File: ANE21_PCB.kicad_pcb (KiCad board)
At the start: 4 copper layers, 59.3 x 63.9 mm, 61 parts, among them J1 Conn_01x02, J13 1-2199119-5, J2 2036150003 (USB-C_Connector), J3 USB-A-S-VT, J5 690-019-298-412, J6 Conn_02x07_Odd_Even, J7 2036150003 (USB-C_Connector), U1 74LVC1G07SE-7, U10 PUSB3FR4, U11 TPD4EUSB30, U12 SI-51005-F, U13 RT9742SNGV, U2 74LVC1G07SE-7, U3 HUSB238_xxxDD, U4 AP62300WU-7, U8 AP62300WU-7, U9 PUSB3FR4

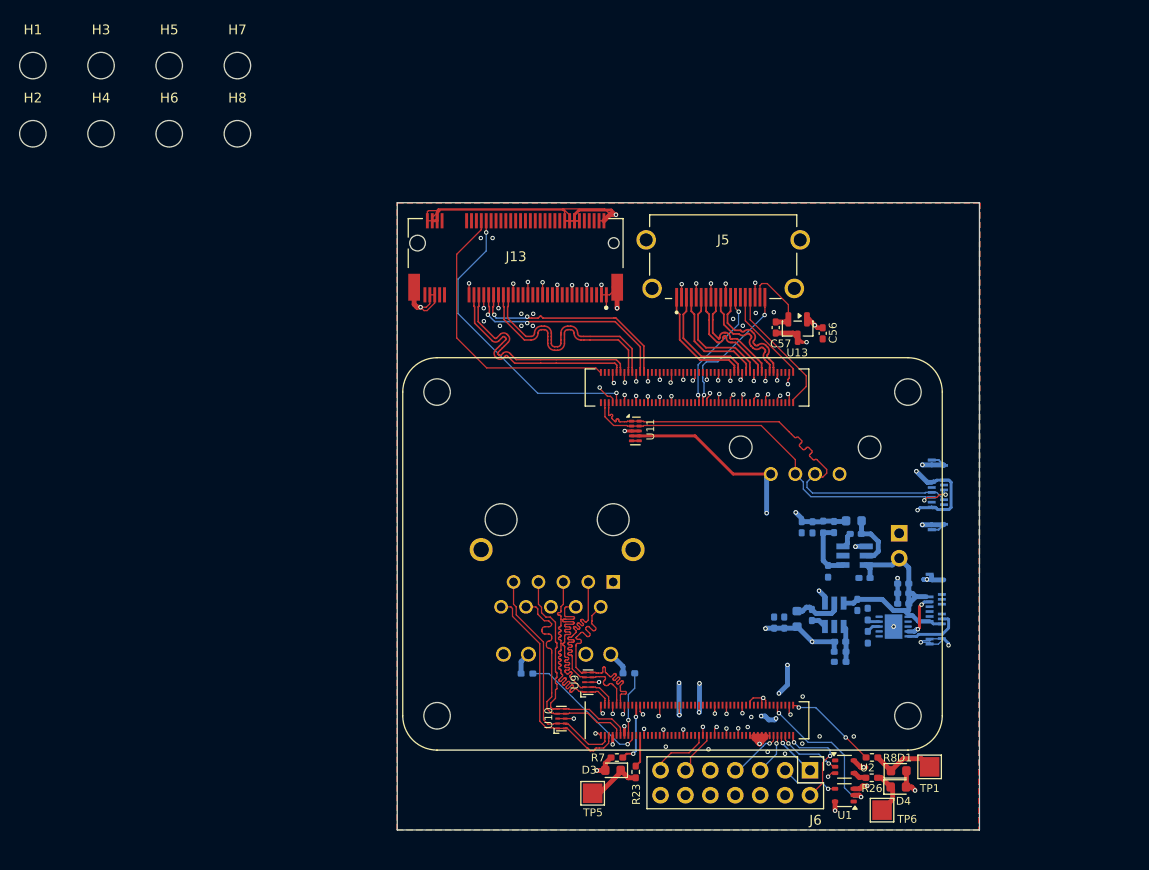
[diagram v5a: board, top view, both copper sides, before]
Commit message: Changed quite a bit, PCB smoll now
Redid all traces, replaced HUSB238 with ch224k, made PCB even smaller.
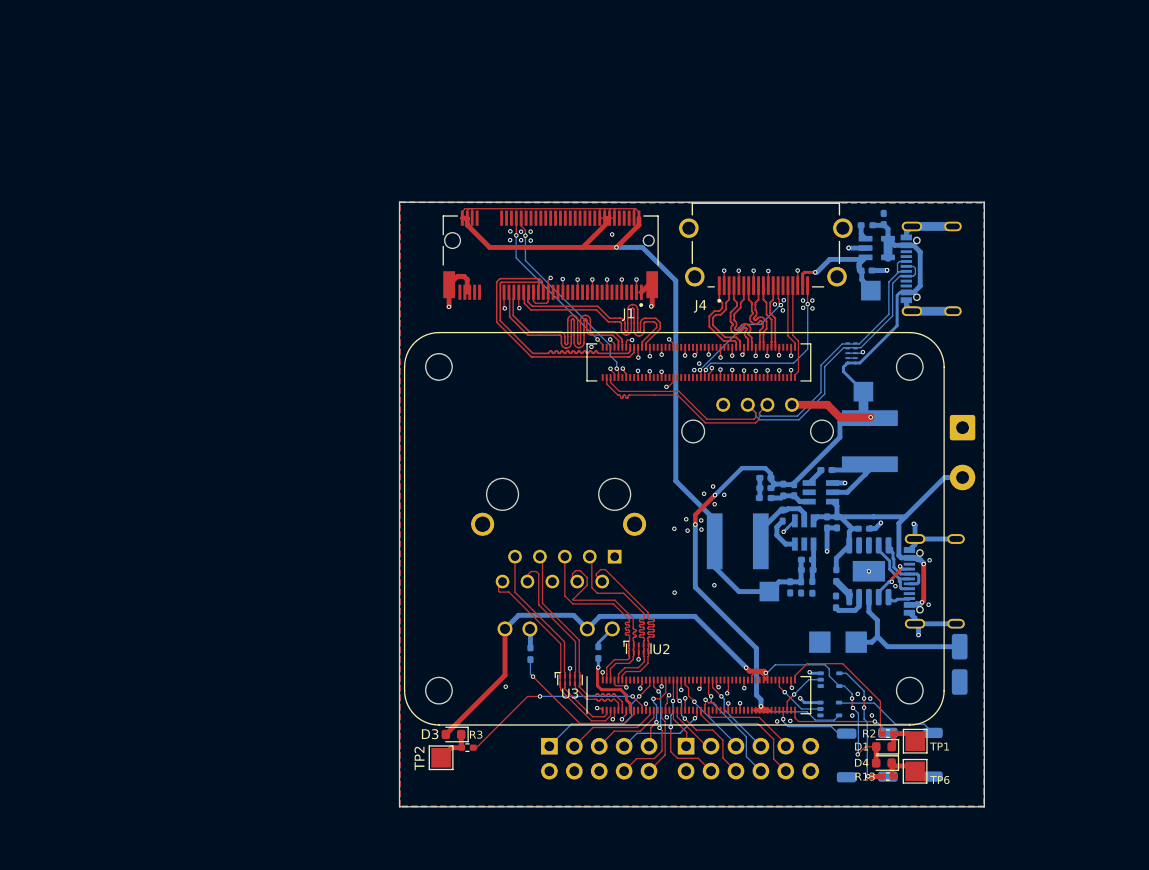
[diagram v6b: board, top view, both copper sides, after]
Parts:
- removed C3: 1µF, Capacitor_SMD:C_0402_1005Metric_Pad0.74x0.62mm_HandSolder
- removed C4, C5: 10µF, Capacitor_SMD:C_0402_1005Metric_Pad0.74x0.62mm_HandSolder
- removed C56, C57: 100n, Capacitor_SMD:C_0402_1005Metric_Pad0.74x0.62mm_HandSolder
- removed H1, H2, H3, H4, H5, H6, H7, H8: MountingHole, MountingHole:MountingHole_2.7mm_M2.5
- removed J13: 1-2199119-5, M2Key:TE_1-2199119-5
- removed J7: 2036150003 (USB-C_Connector), USB-C:CONN_2036150003_MOL(USB-c_connector)
- removed R15, R16: 330, Resistor_SMD:R_0402_1005Metric_Pad0.72x0.64mm_HandSolder
- removed R23, R26, R8: 1k, Resistor_SMD:R_0402_1005Metric_Pad0.72x0.64mm_HandSolder
- removed R7: 10k, Resistor_SMD:R_0402_1005Metric_Pad0.72x0.64mm_HandSolder
- removed U13: RT9742SNGV, Package_TO_SOT_SMD:SOT-23
- added C14: C, Capacitor_SMD:C_0402_1005Metric_Pad0.74x0.62mm_HandSolder, B.Cu at (100.7, 88.2)
- added C15: C, Capacitor_SMD:C_0402_1005Metric_Pad0.74x0.62mm_HandSolder, B.Cu at (101.8, 88.2)
- added C16: 100nF, Capacitor_SMD:C_0402_1005Metric_Pad0.74x0.62mm_HandSolder, B.Cu at (108.2, 82.2)
- added C17: C_Polarized 100uF, Capacitor_SMD:CP_Elec_4x3, B.Cu at (118.0, 96.1)
- added CR1: SMBJ15A, footprints:DIODE_DO214AA, B.Cu at (105.6, 93.8)
- added J4: HDMI_A_1.4, HMDI:AMPHENOL_10029449-111RLF, F.Cu at (98.2, 51.6)
- added J8: Conn_02x06_Odd_Even, Connector_PinHeader_2.54mm:PinHeader_2x06_P2.54mm_Vertical, B.Cu at (90.1, 104.4)
- added R10: R, Resistor_SMD:R_0402_1005Metric_Pad0.72x0.64mm_HandSolder, B.Cu at (98.2, 79.1)
- added R11: R, Resistor_SMD:R_0402_1005Metric_Pad0.72x0.64mm_HandSolder, B.Cu at (102.5, 86.4)
- added R12: R, Resistor_SMD:R_0402_1005Metric_Pad0.72x0.64mm_HandSolder, B.Cu at (103.0, 88.2)
- added R13: R, Resistor_SMD:R_0402_1005Metric_Pad0.72x0.64mm_HandSolder, F.Cu at (110.7, 107.5)
- added R14: 10k, Resistor_SMD:R_0402_1005Metric_Pad0.72x0.64mm_HandSolder, B.Cu at (105.4, 87.0)
- added R9: R, Resistor_SMD:R_0402_1005Metric_Pad0.72x0.64mm_HandSolder, B.Cu at (100.0, 78.3)
- added SW1: SW_Push, Button_Switch_SMD:SW_SPST_TS-1088-xR020, B.Cu at (115.3, 105.3)
- added SW2: SW_Push, Button_Switch_SMD:SW_SPST_TS-1088-xR020, B.Cu at (110.7, 105.3)
- added SW3: SW_Push, Button_Switch_SMD:SW_SPST_TS-1088-xR020, B.Cu at (106.5, 105.3)
- added TP2: TestPoint, TestPoint:TestPoint_Pad_2.0x2.0mm, F.Cu at (65.1, 105.6)
- added TP3: TestPoint, TestPoint:TestPoint_Pad_2.0x2.0mm, B.Cu at (109.0, 58.0)
- added TP4: TestPoint, TestPoint:TestPoint_Pad_2.0x2.0mm, B.Cu at (108.2, 68.3)
- added U5: NCP380HSN05AAT1G, NCP380HSN05AAT1G:SOT95P275X120-5N, B.Cu at (109.6, 53.6)
- added U7: AP62300WU-7, AP62300WU-7:SOT95P280X100-6N, B.Cu at (103.9, 78.5)
- C1, C6, C7: value 100nF -> C
- C10, C11, C12, C13: value 22uF -> C
- C2: value 22µF -> C
- C8, C9: value 10pF -> C
- D1, D3: value LED Green -> LED
- D4: value LED Red -> LED
- J1: value Conn_01x02 -> 1-2199119-5; footprint Connector_PinHeader_2.54mm:PinHeader_1x02_P2.54mm_Vertical -> lib:TE_1-2199119-5; moved to F.Cu
- J2: value 2036150003 (USB-C_Connector) -> USB4105-GF-A; footprint USB-C:CONN_2036150003_MOL(USB-c_connector) -> USB4105-GF-A:GCT_USB4105-GF-A
- J5: value 690-019-298-412 -> Conn_02x05_Odd_Even; footprint HMDI:AMPHENOL_10029449-111RLF -> Connector_PinHeader_2.54mm:PinHeader_2x05_P2.54mm_Vertical; moved to B.Cu
- J6: value Conn_02x07_Odd_Even -> Conn_01x02; footprint Connector_PinHeader_2.54mm:PinHeader_2x07_P2.54mm_Vertical -> TerminalBlock_Phoenix:TerminalBlock_Phoenix_MKDS-1,5-2-5.08_1x02_P5.08mm_Horizontal; moved to B.Cu
- L1, L2: value 3,3uH -> L; footprint Inductor_SMD:L_0603_1608Metric -> 1255AY-3R3N_P3:IND_1255AY-3R3N=P3
- R1: value 10K -> 24k
- R2: value 22.6K -> R; moved to F.Cu
- R3: value 31,6K -> R; moved to F.Cu
- R4: value 10K -> R_Small
- R5: value 52,3K -> R_Small
- R6: value 10K -> R
- TP5: moved to B.Cu
- U1: value 74LVC1G07SE-7 -> SI-51005-F; footprint Package_TO_SOT_SMD:SOT-353_SC-70-5 -> lib:BEL_SI-51005-F; moved to B.Cu
- U10, U9: value PUSB3FR4 -> 74LVC1G07_copy; footprint lib:SOT1176-1 -> Package_TO_SOT_SMD:SOT-353_SC-70-5; moved to B.Cu
- U11: value TPD4EUSB30 -> ~; footprint Package_SON:USON-10_2.5x1.0mm_P0.5mm -> USB4105-GF-A:USB4105-GF-A-PD; moved to B.Cu
- U12: value SI-51005-F -> CH224K; footprint lib:BEL_SI-51005-F -> Package_SO:SSOP-10-1EP_3.9x4.9mm_P1mm_EP2.1x3.3mm
- U2: value 74LVC1G07SE-7 -> PUSB3FR4; footprint Package_TO_SOT_SMD:SOT-353_SC-70-5 -> lib:SOT1176-1
- U3: value HUSB238_xxxDD -> PUSB3FR4; footprint Package_DFN_QFN:WDFN-10-1EP_3x3mm_P0.5mm_EP1.8x2.5mm -> lib:SOT1176-1; moved to F.Cu
- U4: value AP62300WU-7 -> PUSB3FR4; footprint AP62300WU-7:SOT95P280X100-6N -> lib:SOT1176-1
- moved J5 54.6 mm to (76.2, 104.4), turned to -90 degrees
- moved J1 45.5 mm to (76.3, 54.4)
- moved R6 44.6 mm to (108.6, 51.3)
- moved R3 42.7 mm to (67.8, 104.5), turned to 180 degrees
- moved U1 42.3 mm to (77.1, 78.7), turned to 0 degrees
- moved U11 40.1 mm to (121.9, 87.8), turned to -90 degrees
- moved C1 39.3 mm to (110.3, 50.7), turned to 90 degrees
- moved J6 38.2 mm to (118.3, 71.9)
- moved U3 33.4 mm to (78.3, 97.7), turned to 0 degrees
- moved C2 33.1 mm to (108.5, 55.9)
- moved U12 32.2 mm to (108.8, 86.6), turned to -90 degrees
- moved R5 31.6 mm to (74.2, 95.0), turned to -90 degrees
- moved U10 27.7 mm to (104.8, 97.6), turned to 0 degrees
- moved TP5 27.3 mm to (98.6, 88.6)
- moved R4 24.8 mm to (81.2, 94.9), turned to 90 degrees
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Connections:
- net /CM4_LowSpeed/GPIO4 renamed /CM4_LowSpeed/GPIO4_GPCLK0
- C1 pad 1: GND -> VBUS
- C1 pad 2: /+12v -> GND
- C10 pad 2: /+3.3v -> VBUS
- C11 pad 1: GND -> VBUS-PD
- C11 pad 2: /+5v -> GND
- C12 pad 1: GND -> Net-(U8-BST)
- C12 pad 2: /+3.3v -> Net-(U8-SW)
- C13 pad 1: GND -> Net-(U8-FB)
- C13 pad 2: /+5v -> /+3.3v
- C2 pad 1: GND -> HDMI_5v
- C2 pad 2: /+12v -> GND
- C6 pad 1: Net-(U4-BST) -> VBUS-PD
- C6 pad 2: Net-(U4-SW) -> GND
- C7 pad 1: Net-(U8-BST) -> Net-(U7-BST)
- C7 pad 2: Net-(U8-SW) -> Net-(U7-SW)
- C8 pad 1: Net-(U4-FB) -> Net-(U7-FB)
- C8 pad 2: /+3.3v -> VBUS
- C9 pad 1: Net-(U8-FB) -> GND
- C9 pad 2: /+5v -> VBUS
- J1 pad 2: /+12v -> /+3.3v
- J3 pad 1: /+5v -> VBUS
- J5 pad 1: /CM4_HighSpeed/HDMI0_D2_P -> /CM4_LowSpeed/GPIO19_PCM_FS
- J5 pad 10: /CM4_HighSpeed/HDMI0_CK_P -> /CM4_LowSpeed/GPIO12_PWM0_0
- J5 pad 3: /CM4_HighSpeed/HDMI0_D2_N -> /CM4_LowSpeed/GPIO21_PCM_DOUT
- J5 pad 4: /CM4_HighSpeed/HDMI0_D1_P -> GND
- J5 pad 5: GND -> /CM4_LowSpeed/GPIO20_PCM_DIN
- J5 pad 6: /CM4_HighSpeed/HDMI0_D1_N -> GND
- J5 pad 7: /CM4_HighSpeed/HDMI0_D0_P -> /CM4_LowSpeed/GPIO18_PCM_CLK
- J5 pad 8: GND -> /CM4_LowSpeed/GPIO13_PWM0_1
- J5 pad 9: /CM4_HighSpeed/HDMI0_D0_N -> /CM4_LowSpeed/GPIO5_GPCLK1
- J6 pad 1: /CM4_LowSpeed/nRPIBOOT -> GND
- J6 pad 2: /CM4_LowSpeed/GLOBAL_EN -> VBUS-PD
- L1 pad 1: Net-(U4-SW) -> Net-(U8-SW)
- L2 pad 1: Net-(U8-SW) -> Net-(U7-SW)
- L2 pad 2: /+5v -> VBUS
- Module1 pad 20: Net-(Module1A-EEPROM_nWP) -> unconnected-(Module1A-EEPROM_nWP-Pad20)
- Module1 pad 24: /CM4_LowSpeed/GPIO26 -> unconnected-(Module1A-GPIO26-Pad24)
- Module1 pad 25: /CM4_LowSpeed/GPIO21 -> /CM4_LowSpeed/GPIO21_PCM_DOUT
- Module1 pad 26: /CM4_LowSpeed/GPIO19 -> /CM4_LowSpeed/GPIO19_PCM_FS
- Module1 pad 27: /CM4_LowSpeed/GPIO20 -> /CM4_LowSpeed/GPIO20_PCM_DIN
- Module1 pad 28: /CM4_LowSpeed/GPIO13 -> /CM4_LowSpeed/GPIO13_PWM0_1
- Module1 pad 29: /CM4_LowSpeed/GPIO16 -> unconnected-(Module1A-GPIO16-Pad29)
- Module1 pad 30: /CM4_LowSpeed/GPIO6 -> unconnected-(Module1A-GPIO6-Pad30)
- Module1 pad 31: /CM4_LowSpeed/GPIO12 -> /CM4_LowSpeed/GPIO12_PWM0_0
- Module1 pad 34: /CM4_LowSpeed/GPIO5 -> /CM4_LowSpeed/GPIO5_GPCLK1
- Module1 pad 37: /CM4_LowSpeed/GPIO7 -> /CM4_LowSpeed/GPIO7_SPI0_CE1_N
- Module1 pad 38: /CM4_LowSpeed/GPIO11 -> /CM4_LowSpeed/GPIO11_SPI0_SCLK
- Module1 pad 39: /CM4_LowSpeed/GPIO8 -> /CM4_LowSpeed/GPIO8_SPI0_CE0_N
- Module1 pad 40: /CM4_LowSpeed/GPIO9 -> /CM4_LowSpeed/GPIO9_SPI0_MISO
- Module1 pad 41: /CM4_LowSpeed/GPIO25 -> unconnected-(Module1A-GPIO25-Pad41)
- Module1 pad 44: /CM4_LowSpeed/GPIO10 -> /CM4_LowSpeed/GPIO10_SPI0_MOSI
- Module1 pad 45: /CM4_LowSpeed/GPIO24 -> unconnected-(Module1A-GPIO24-Pad45)
- Module1 pad 46: /CM4_LowSpeed/GPIO22 -> unconnected-(Module1A-GPIO22-Pad46)
- Module1 pad 47: /CM4_LowSpeed/GPIO23 -> unconnected-(Module1A-GPIO23-Pad47)
- Module1 pad 48: /CM4_LowSpeed/GPIO27 -> unconnected-(Module1A-GPIO27-Pad48)
- Module1 pad 49: /CM4_LowSpeed/GPIO18 -> /CM4_LowSpeed/GPIO18_PCM_CLK
- Module1 pad 50: /CM4_LowSpeed/GPIO17 -> unconnected-(Module1A-GPIO17-Pad50)
- Module1 pad 51: /GPIO15 -> /GPIO15_RXD0
- Module1 pad 55: /GPIO14 -> /GPIO14_TXD0
- Module1 pad 56: /CM4_LowSpeed/GPIO3 -> /CM4_LowSpeed/GPIO3_SCL1
- Module1 pad 58: /CM4_LowSpeed/GPIO2 -> /CM4_LowSpeed/GPIO2_SDA1
- Module1 pad 77: /+5v -> VBUS
- Module1 pad 79: /+5v -> VBUS
- Module1 pad 81: /+5v -> VBUS
- Module1 pad 83: /+5v -> VBUS
- Module1 pad 85: /+5v -> VBUS
- Module1 pad 87: /+5v -> VBUS
- R1 pad 1: Net-(U3-VSET) -> Net-(U12-CFG1)
- R2 pad 1: Net-(U3-ISET) -> Net-(Module1A-nEXTRST)
- R2 pad 2: GND -> Net-(D1-K)
- R3 pad 1: /+3.3v -> Net-(Module1A-PI_nLED_Activity)
- R3 pad 2: Net-(U4-FB) -> Net-(D3-K)
- R4 pad 1: Net-(U4-FB) -> /CM4_LowSpeed/LEDG
- R4 pad 2: GND -> Net-(U1-LEDR_K)
- R5 pad 1: /+5v -> Net-(U1-LEDL_K)
- R5 pad 2: Net-(U8-FB) -> /CM4_LowSpeed/LEDY
- R6 pad 1: Net-(U8-FB) -> VBUS
- R6 pad 2: GND -> Net-(U5-*FLAG)
- TP5 pad 1: Net-(D3-K) -> /+3.3v
- U1 pad 2: /CM4_LowSpeed/RUN_PG -> /CM4_LowSpeed/TRD0_P
- U1 pad 3: GND -> /CM4_LowSpeed/TRD0_N
- U1 pad 4: /Miscellaneous/Reset -> /CM4_LowSpeed/TRD1_P
- U1 pad 5: /+5v -> /CM4_LowSpeed/TRD1_N
- U10 pad 1: /CM4_LowSpeed/TRD3_N -> (no net)
- U10 pad 2: /CM4_LowSpeed/TRD3_P -> /CM4_LowSpeed/nPWR_LED
- U10 pad 4: /CM4_LowSpeed/TRD2_N -> Net-(R13-Pad2)
- U10 pad 5: /CM4_LowSpeed/TRD2_P -> /3.3V OUT (CM4.86)
- U12 pad 1: GND -> VBUS-PD
- U12 pad 10: /CM4_LowSpeed/TRD3_N -> Net-(U12-PG)
- U12 pad 2: /CM4_LowSpeed/TRD0_P -> unconnected-(U12-CFG2-Pad2)
- U12 pad 3: /CM4_LowSpeed/TRD0_N -> unconnected-(U12-CFG3-Pad3)
- U12 pad 4: /CM4_LowSpeed/TRD1_P -> DP1
- U12 pad 5: /CM4_LowSpeed/TRD1_N -> DN1
- U12 pad 6: unconnected-(U12-CT-Pad6) -> CC2_U9
- U12 pad 7: /CM4_LowSpeed/TRD2_P -> CC1_U9
- U12 pad 8: /CM4_LowSpeed/TRD2_N -> Net-(U12-VBUS)
- U12 pad 9: /CM4_LowSpeed/TRD3_P -> Net-(U12-CFG1)
- U2 pad 2: /CM4_LowSpeed/nPWR_LED -> /CM4_LowSpeed/TRD1_P
- U2 pad 4: Net-(R26-Pad2) -> /CM4_LowSpeed/TRD0_N
- U2 pad 5: /3.3V OUT (CM4.86) -> /CM4_LowSpeed/TRD0_P
- U3 pad 1: /+12v -> /CM4_LowSpeed/TRD3_N
- U3 pad 10: unconnected-(U3-GATE-Pad10) -> /CM4_LowSpeed/TRD3_N
- U3 pad 2: unconnected-(U3-D+-Pad2) -> /CM4_LowSpeed/TRD3_P
- U3 pad 3: unconnected-(U3-D--Pad3) -> GND
- U3 pad 4: CC1_U9 -> /CM4_LowSpeed/TRD2_N
- U3 pad 5: CC2_U9 -> /CM4_LowSpeed/TRD2_P
- U3 pad 6: unconnected-(U3-SDA-Pad6) -> /CM4_LowSpeed/TRD2_P
- U3 pad 7: unconnected-(U3-SCL-Pad7) -> /CM4_LowSpeed/TRD2_N
- U3 pad 8: Net-(U3-VSET) -> GND
- U3 pad 9: Net-(U3-ISET) -> /CM4_LowSpeed/TRD3_P
- U4 pad 1: GND -> VBUS
- U4 pad 2: Net-(U4-SW) -> unconnected-(U4-In_1--Pad2)
- U4 pad 3: /+12v -> GND
- U4 pad 4: Net-(U4-FB) -> USBD+
- U4 pad 5: unconnected-(U4-EN-Pad5) -> USBD-
- U4 pad 6: Net-(U4-BST) -> USBD-
- U8 pad 3: /+12v -> VBUS-PD
- U9 pad 1: /CM4_LowSpeed/TRD1_N -> (no net)
- U9 pad 2: /CM4_LowSpeed/TRD1_P -> /CM4_LowSpeed/RUN_PG
- U9 pad 4: /CM4_LowSpeed/TRD0_N -> /Miscellaneous/Reset
- U9 pad 5: /CM4_LowSpeed/TRD0_P -> VBUS
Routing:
- net /+5v: track 122.4 -> 0.00 mm, vias 10 -> 0
- net VBUS: track 0.00 -> 99.0 mm, vias 0 -> 4
- net VBUS-PD: track 0.00 -> 38.5 mm, vias 0 -> 2
- net /+12v: track 25.2 -> 0.00 mm
- net Net-(Module1A-PI_nLED_Activity): track 3.32 -> 20.2 mm, vias 0 -> 2
- net Net-(U12-VBUS): track 0.00 -> 15.6 mm
- net /3.3V OUT (CM4.86): track 85.6 -> 70.7 mm, vias 4 -> 5
- net /CM4_LowSpeed/GPIO19_PCM_FS: track 0.00 -> 14.1 mm, vias 0 -> 1
- net Net-(R13-Pad2): track 0.00 -> 13.5 mm, vias 0 -> 3
- net /CM4_LowSpeed/GPIO9_SPI0_MISO: track 0.00 -> 12.8 mm, vias 0 -> 2
- net /GPIO15_RXD0: track 0.00 -> 12.7 mm
- net /CM4_LowSpeed/GPIO11_SPI0_SCLK: track 0.00 -> 12.3 mm, vias 0 -> 2
- net /CM4_HighSpeed/P_CLKnREQ: track 29.2 -> 16.8 mm, vias 0 -> 2
- net /CM4_LowSpeed/GPIO13_PWM0_1: track 0.00 -> 12.1 mm, vias 0 -> 2
- net /CM4_LowSpeed/GPIO3_SCL1: track 0.00 -> 11.5 mm, vias 0 -> 1
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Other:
- board size 59.3 x 63.9 mm -> 59.6 x 61.6 mm
- board text added: "*"
- board text added: "Boot"
- board text added: "CE0"
- board text added: "CE1"
- board text added: "CLK"
- board text added: "DIN"
- board text added: "DOUT"
- board text added: "FS"
- board text added: "GCLK1"
- board text added: "GND"
- board text added: "Glb_EN"
- board text added: "MOSI"
- board text added: "PWM0|1"
- board text added: "RX|SCL|MISO|CLK|G"
- board text added: "Reset"
- board text added: "SDA"
- board text added: "TX"

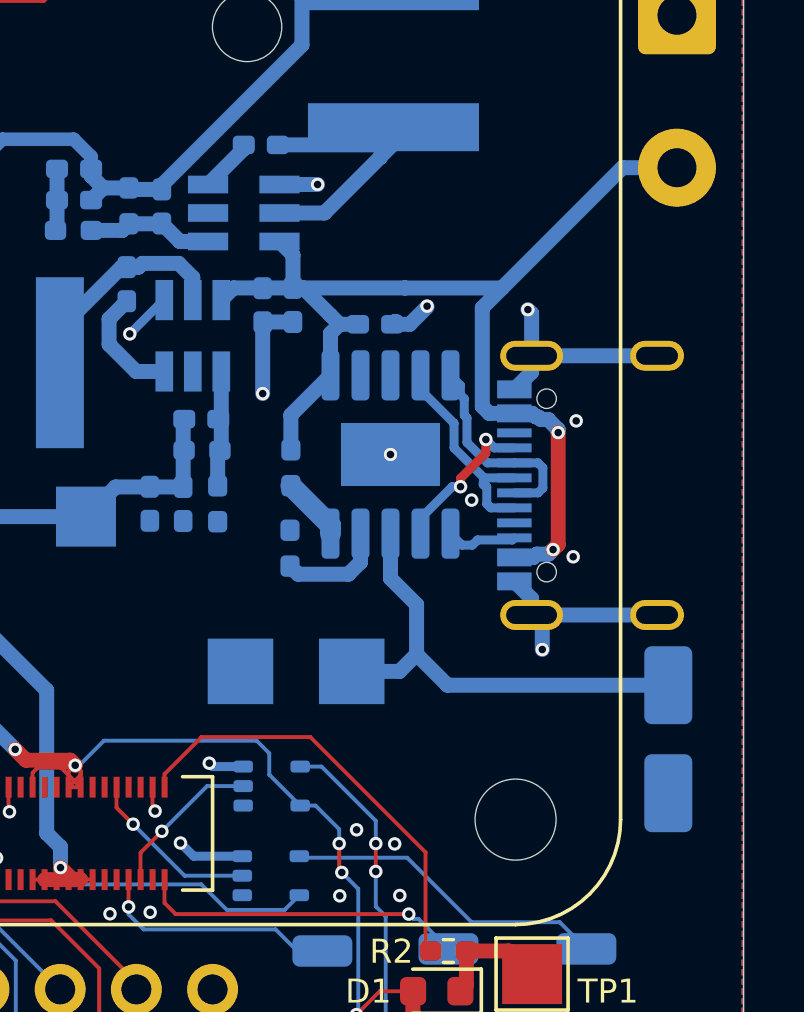
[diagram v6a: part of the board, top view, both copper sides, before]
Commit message: Changed PD back to HUSB238
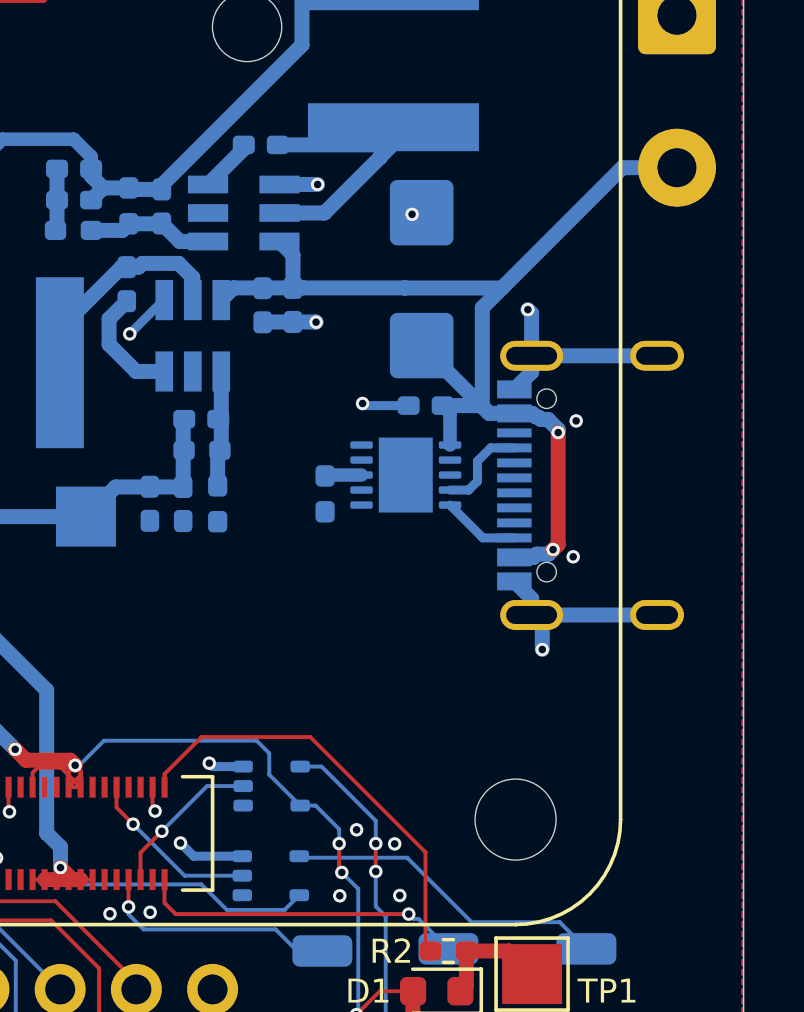
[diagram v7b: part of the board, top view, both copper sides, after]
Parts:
- removed C16: 100nF, Capacitor_SMD:C_0402_1005Metric_Pad0.74x0.62mm_HandSolder
- removed C17: C_Polarized 100uF, Capacitor_SMD:CP_Elec_4x3
- removed CR1: SMBJ15A, footprints:DIODE_DO214AA
- removed R1: 24k, Resistor_SMD:R_0402_1005Metric_Pad0.72x0.64mm_HandSolder
- removed R14: 10k, Resistor_SMD:R_0402_1005Metric_Pad0.72x0.64mm_HandSolder
- removed U12: CH224K, Package_SO:SSOP-10-1EP_3.9x4.9mm_P1mm_EP2.1x3.3mm
- added C3: 1µF, Capacitor_SMD:C_0402_1005Metric_Pad0.74x0.62mm_HandSolder, B.Cu at (109.9, 84.9)
- added D2: SMBJ14A, SMBJ14A:DIOM5436X261N, B.Cu at (109.8, 80.7)
- added R7: 10K, Resistor_SMD:R_0402_1005Metric_Pad0.72x0.64mm_HandSolder, B.Cu at (106.6, 87.9)
- added U6: HUSB238_xxxDD, Package_DFN_QFN:WDFN-10-1EP_3x3mm_P0.5mm_EP1.8x2.5mm, B.Cu at (109.3, 87.3)
- C11, C6: value C -> 10uF
- C12, C7: value C -> 100nF
- L1, L2: value L -> 3.3uH
- R10, R12: value R -> 10k
- R11: value R -> 31.6k
- R9: value R -> 52.3k
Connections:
- U11 pad B6: DP1 -> DP2
- U11 pad B7: DN1 -> DN2
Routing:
- net Net-(U12-VBUS): track 15.6 -> 0.00 mm
- net DP1: track 7.08 -> 0.00 mm
- net DN1: track 7.04 -> 0.00 mm
- net Net-(U12-CFG1): track 3.58 -> 0.00 mm
- net CC1_U9: track 5.27 -> 3.12 mm, vias 2 -> 0
- net Net-(U12-PG): track 2.14 -> 0.00 mm
- net GND: track 130.2 -> 128.6 mm, vias 118 -> 117
- net VBUS-PD: track 38.5 -> 37.2 mm
- net Net-(U6-VSET): track 0.00 -> 1.23 mm

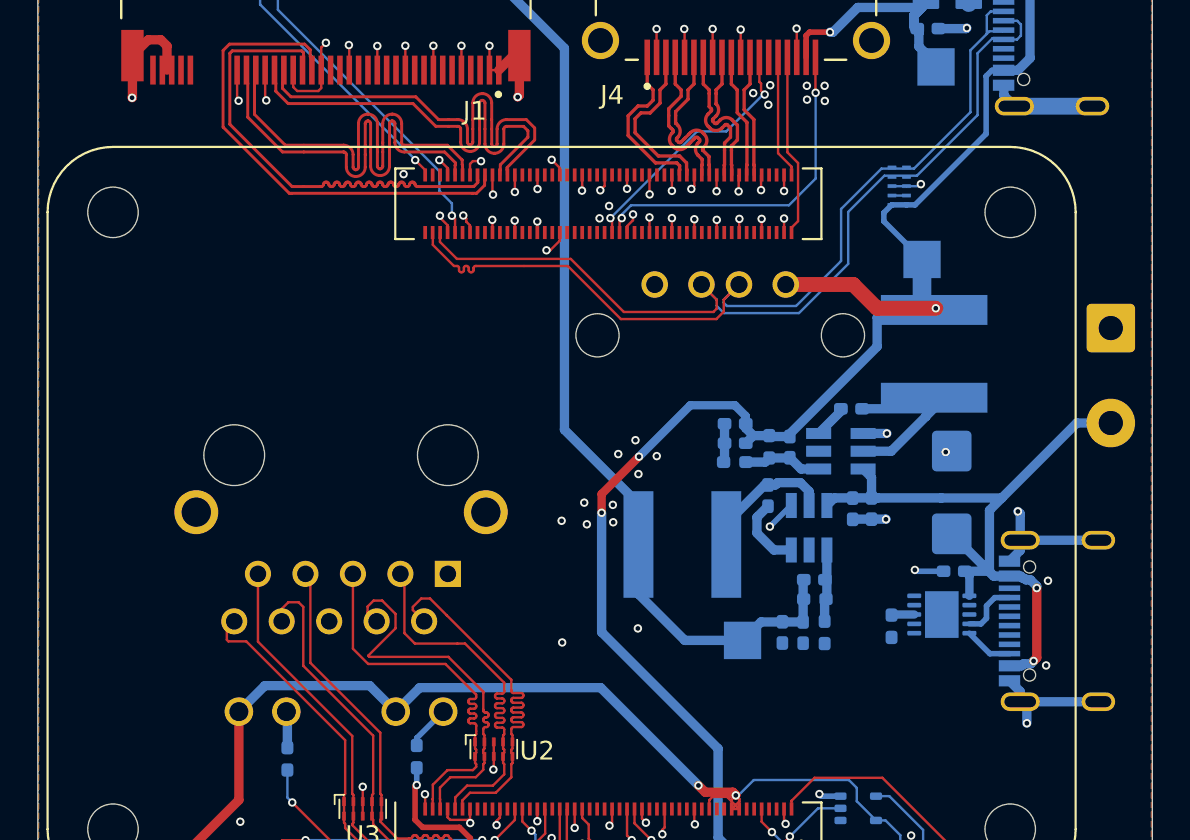
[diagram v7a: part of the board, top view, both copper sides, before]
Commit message: Adjusted footprint Phoenix connector and added some text.
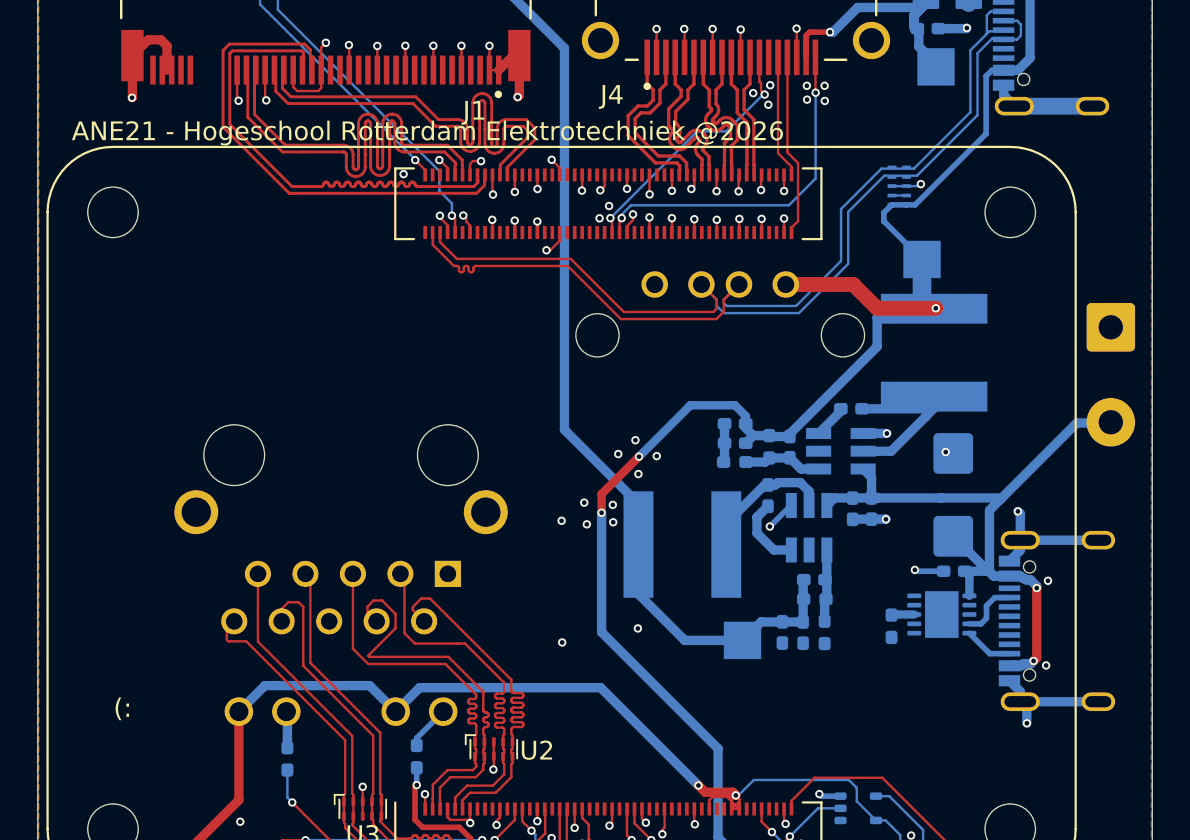
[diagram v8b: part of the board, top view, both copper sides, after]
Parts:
- J6: footprint TerminalBlock_Phoenix:TerminalBlock_Phoenix_MKDS-1,5-2-5.08_1x02_P5.08mm_Horizontal -> 1-2199119-5_Finley:TerminalBlock_PhoenixTerminalBlock_Phoenix_MKDS-1,5-2-5.08_1x02_P5.08mm_Horizontal_Edited
- moved J6 3.94 mm to (115.9, 75.1)
- moved D2 0.15 mm to (109.9, 80.9)
- moved L2 0.06 mm to (108.8, 73.2)
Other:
- board text added: "(:"
- board text added: "ANE21 - Hogeschool Rotterdam Elektrotechniek @2026"
- board text added: "Jochem.R Deniz.D"
